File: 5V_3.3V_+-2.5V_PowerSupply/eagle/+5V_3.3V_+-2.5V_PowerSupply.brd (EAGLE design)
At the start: 100 x 80 mm, 55 parts, among them IC1 7805TV, IC2 LM4558N, IC3 TA48033S, SW1 PUSH_SW_ALT

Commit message: Update: 5V_3V3_2V5_PowerSupply Eagle Files
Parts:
- removed SL1: PWRIN+, con-amp-quick:02P
- removed SL2: PWRIN-, con-amp-quick:02P
- removed U$1, U$2: POLYSWITCH, mylib2:POLYSWITCH
- added JP21: TP_GND, pinhead:1X02
- added PS1, PS2: POLYSWITCH-5,0, mylib2:POLYSWITCH-5,0
- added X1: PWR-, con-wago-500:W237-102
- added X2: PWR+, con-wago-500:W237-102
- C1, C11, C2: device rcl:C050-025X075 -> rcl:C025-024X044
- C10, C9: device rcl:E2,5-6 -> rcl:E2,5-7
- C5: device rcl:C050-024X044 -> rcl:C025-024X044
- IC2: value LM4558N -> LM4556
- JP15, JP17, JP18, JP3, JP4: value +3.3V -> +2.5V
- LED1, LED4, LED5: value (none) -> GREEN
- LED2: value (none) -> RED
- LED3: value (none) -> BLUE
- moved JP20 310.4 mm to (86.4, 55.9), turned to 270 degrees
- moved JP19 302.5 mm to (83.8, 55.9), turned to 270 degrees
- moved LED5 243.2 mm to (50.8, 14.0), turned to 270 degrees
- moved R7 232.3 mm to (47.0, 10.2), turned to 180 degrees
- moved LED4 230.7 mm to (24.1, 30.5), turned to 180 degrees
- moved C6 224.6 mm to (47.0, 20.3), turned to 180 degrees
- moved JP18 222.0 mm to (86.4, 19.1), turned to 90 degrees
- moved R6 219.0 mm to (26.7, 10.2)
- moved JP15 213.0 mm to (81.3, 19.1), turned to 90 degrees
- moved JP17 209.6 mm to (83.8, 19.1), turned to 90 degrees
- moved C4 207.9 mm to (27.9, 19.1), turned to 270 degrees
- moved C2 205.4 mm to (45.7, 14.0), turned to 270 degrees
- moved JP3 203.9 mm to (76.2, 19.1), turned to 90 degrees
- moved JP4 200.5 mm to (78.7, 19.1), turned to 90 degrees
- moved C1 196.8 mm to (33.0, 19.1), turned to 270 degrees
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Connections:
- new net V+: C1.2, C2.1, C4.-, C6.+, IC2.1, IC2.2, JP15.1, JP17.1, JP18.1, JP3.1, JP4.1, LED5.A
- net +3V3: no longer C1.2, C2.1, C4.-, C6.+, IC2.1, IC2.2, JP15.1, JP17.1, JP18.1, JP3.1, JP4.1, LED5.A
- net +9V: now also JP19.1, JP20.1, R2.1; no longer LED2.A
- net -9V: now also JP19.3, JP20.3
- net GND: now also JP19.2, JP20.2, JP21.1, JP21.2, LED2.K, X1.1, X2.2; no longer R2.2, SL1.1, SL2.2
- net N$1: now also PS2.2, X2.1; no longer SL2.1, U$2.2
- net N$10: now also PS1.2, X1.2; no longer SL1.2, U$1.2
- net N$11: now also PS2.1, SW1.3; no longer SW1.4, U$2.1
- net N$2: now also PS1.1, SW1.6; no longer SW1.1, U$1.1
- net N$4: now also LED2.A, R2.2; no longer LED2.K, R2.1
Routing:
- net +9V: track 0.00 -> 5.08 mm
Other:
- board size 100 x 80 mm -> 93.7 x 71.1 mm

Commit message: Update: Eagle files
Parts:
- removed JP16, JP19, JP20: +-9V, pinhead:1X03
- removed JP17, JP18: +2.5V, pinhead:1X02
- JP10, JP9: value +3.3V -> +5V_2V5; device pinhead:1X02 -> pinhead:1X03
- JP13: value +5V -> +3.3V
- JP15: value +2.5V -> +3.3V
- JP3, JP4: value +2.5V -> +-9V; device pinhead:1X02 -> pinhead:1X03
- JP5: value +5V -> +-9V; device pinhead:1X02 -> pinhead:1X03
- JP6, JP7, JP8: value +5V -> +5V_2V5; device pinhead:1X02 -> pinhead:1X03
- moved JP3 30.2 mm to (68.6, 48.3), turned to 270 degrees
- moved JP4 30.2 mm to (71.1, 48.3), turned to 270 degrees
- moved JP13 23.4 mm to (68.6, 24.1), turned to 270 degrees
- moved R4 20.1 mm to (41.9, 10.2), turned to 180 degrees
- moved R6 19.1 mm to (25.4, 29.2), turned to 90 degrees
- moved JP11 18.5 mm to (63.5, 24.1), turned to 270 degrees
- moved JP12 18.5 mm to (66.0, 24.1), turned to 270 degrees
- moved JP10 16.5 mm to (63.5, 35.6), turned to 270 degrees
- moved JP14 16.1 mm to (71.1, 24.1), turned to 270 degrees
- moved JP8 15.7 mm to (68.6, 35.6), turned to 270 degrees
- moved JP1 14.8 mm to (63.5, 48.3)
- moved JP2 14.8 mm to (66.0, 48.3)
- moved C10 14.5 mm to (54.6, 53.3), turned to 0 degrees
- moved R7 13.7 mm to (59.7, 15.2)
- moved LED5 13.0 mm to (63.5, 11.4), turned to 90 degrees
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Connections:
- net +3V3: now also JP13.1, JP15.1; no longer JP10.1, JP9.1
- net +5V: now also JP10.1, JP9.1; no longer JP13.1, JP5.1
- net +9V: now also JP3.1, JP4.1, JP5.1; no longer JP16.1, JP19.1, JP20.1
- net -9V: now also JP3.3, JP4.3, JP5.3; no longer JP16.3, JP19.3, JP20.3
- net GND: now also JP10.3, JP6.3, JP7.3, JP8.3, JP9.3; no longer JP10.2, JP16.2, JP17.2, JP18.2, JP19.2, JP20.2, JP6.2, JP7.2, JP8.2, JP9.2
- net V+: now also JP10.2, JP6.2, JP7.2, JP8.2, JP9.2; no longer JP15.1, JP17.1, JP18.1, JP3.1, JP4.1
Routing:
- net GND: track 0.00 -> 374.2 mm
- net +5V: track 0.00 -> 159.8 mm, vias 0 -> 4
- net V+: track 0.00 -> 96.1 mm, vias 0 -> 2
- net -9V: track 0.00 -> 88.5 mm
- net +9V: track 5.08 -> 77.9 mm
- net +3V3: track 0.00 -> 63.1 mm, vias 0 -> 2
- net N$2: track 0.00 -> 20.3 mm
- net N$5: track 0.00 -> 17.3 mm
- net N$11: track 0.00 -> 12.2 mm
- net N$10: track 0.00 -> 5.25 mm
- net N$1: track 0.00 -> 5.25 mm
- net N$7: track 0.00 -> 5.08 mm
- net N$12: track 0.00 -> 2.54 mm
- net N$8: track 0.00 -> 2.54 mm
- net N$9: track 0.00 -> 2.54 mm
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
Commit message: Update: Board design
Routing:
- net +5V: track 159.8 -> 160.8 mm
- net V+: track 96.1 -> 97.1 mm
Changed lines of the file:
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@@
 <wire x1="35.56" y1="35.56" x2="40.64" y2="35.56" width="0.4064" layer="16"/>
 <wire x1="38.1" y1="20.32" x2="40.64" y2="20.32" width="0.4064" layer="16"/>
-<wire x1="33.02" y1="20.32" x2="30.48" y2="20.32" width="0.4064" layer="16"/>
-<wire x1="30.48" y1="20.32" x2="30.48" y2="15.24" width="0.4064" layer="16"/>
-<wire x1="30.48" y1="15.24" x2="35.56" y2="10.16" width="0.4064" layer="16"/>
-<wire x1="35.56" y1="10.16" x2="38.1" y2="10.16" width="0.4064" layer="16"/>
 <wire x1="33.02" y1="20.32" x2="38.1" y2="20.32" width="0.4064" layer="16"/>
-<wire x1="40.64" y1="20.32" x2="40.64" y2="22.86" width="0.4064" layer="16"/>
-<wire x1="40.64" y1="22.86" x2="22.86" y2="22.86" width="0.4064" layer="16"/>
 <wire x1="22.86" y1="22.86" x2="22.86" y2="35.56" width="0.4064" layer="1"/>
 <wire x1="22.86" y1="35.56" x2="35.56" y2="35.56" width="0.4064" layer="16"/>
@@
 <wire x1="48.26" y1="55.88" x2="50.8" y2="55.88" width="0.4064" layer="16"/>
 <wire x1="50.8" y1="55.88" x2="53.34" y2="53.34" width="0.4064" layer="16"/>
+<wire x1="38.1" y1="10.16" x2="30.48" y2="10.16" width="0.4064" layer="16"/>
+<wire x1="22.86" y1="22.86" x2="22.86" y2="20.32" width="0.4064" layer="16"/>
+<wire x1="22.86" y1="20.32" x2="22.86" y2="17.78" width="0.4064" layer="16"/>
+<wire x1="22.86" y1="17.78" x2="30.48" y2="10.16" width="0.4064" layer="16"/>
+<wire x1="38.1" y1="20.32" x2="22.86" y2="20.32" width="0.4064" layer="16"/>
 </signal>
 <signal name="+3V3">
@@
 <contactref element="C6" pad="+"/>
 <wire x1="43.18" y1="12.7" x2="40.64" y2="12.7" width="0.4064" layer="16"/>
-<wire x1="43.18" y1="12.7" x2="43.18" y2="5.08" width="0.4064" layer="16"/>
 <wire x1="43.18" y1="5.08" x2="48.26" y2="5.08" width="0.4064" layer="16"/>
 <wire x1="48.26" y1="5.08" x2="50.8" y2="7.62" width="0.4064" layer="16"/>
@@
 <wire x1="63.5" y1="35.56" x2="58.42" y2="35.56" width="0.4064" layer="16"/>
 <wire x1="58.42" y1="35.56" x2="58.42" y2="27.94" width="0.4064" layer="16"/>
+<wire x1="43.18" y1="5.08" x2="40.64" y2="7.62" width="0.4064" layer="16"/>
+<wire x1="40.64" y1="7.62" x2="40.64" y2="12.7" width="0.4064" layer="16"/>
 </signal>
 <signal name="N$2">

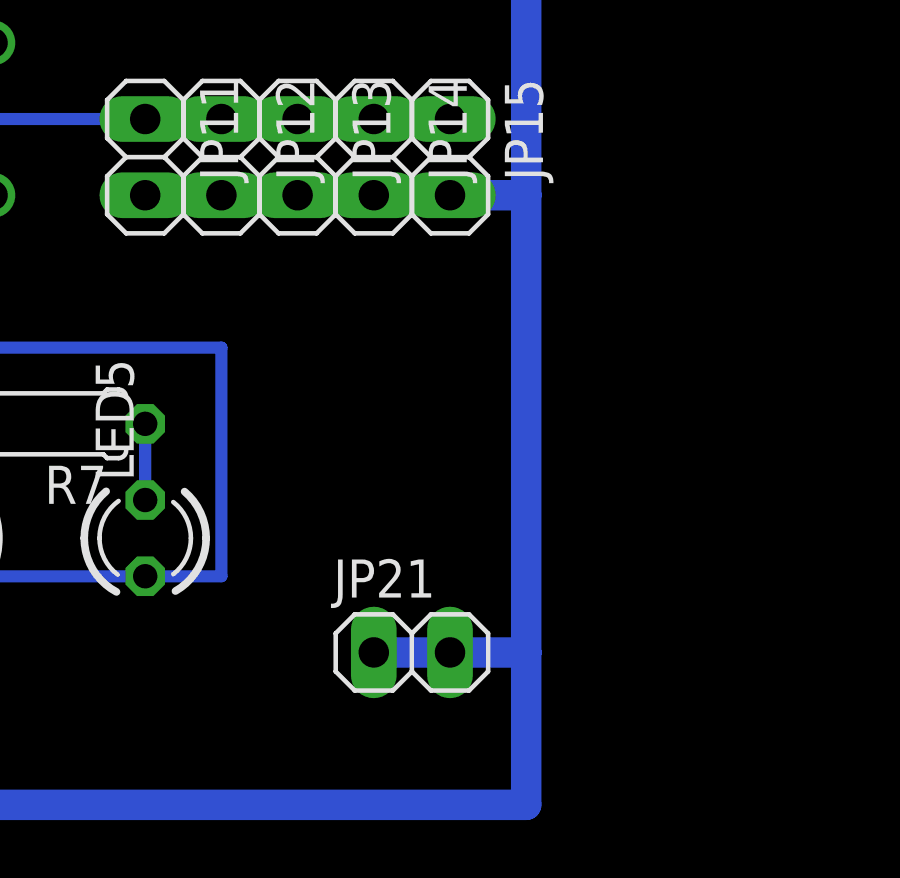
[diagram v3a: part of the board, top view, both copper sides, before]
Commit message: Add: 5V_3.3V_+-2.5V_PowerSupply Test Chart
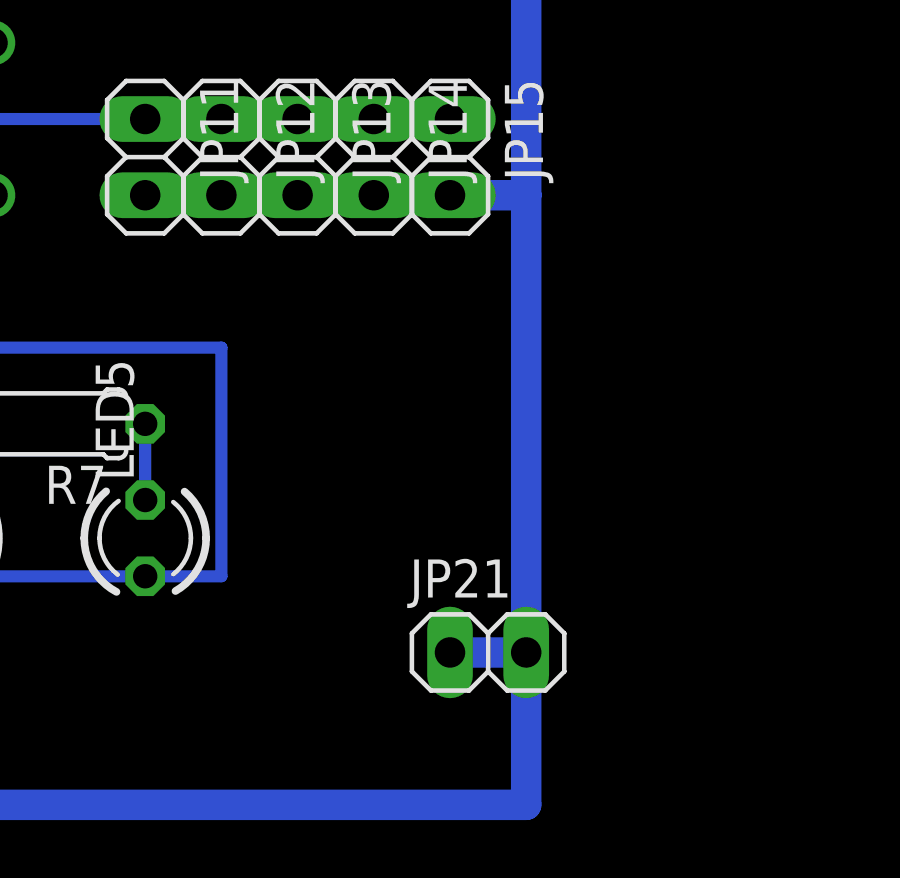
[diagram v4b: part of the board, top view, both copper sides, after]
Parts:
- moved JP21 2.54 mm to (74.9, 7.62)
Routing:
- net GND: track 374.2 -> 371.7 mm
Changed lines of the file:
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@@
 <attribute name="OC_FARNELL" value="unknown" x="8.89" y="53.34" size="1.778" layer="27" rot="R270" display="off"/>
 </element>
-<element name="JP21" library="pinhead" package="1X02" value="TP_GND" x="72.39" y="7.62"/>
+<element name="JP21" library="pinhead" package="1X02" value="TP_GND" x="74.93" y="7.62"/>
 <element name="SW1" library="mylib2" package="PUSH_SW_ALT" value="PUSH_SW_ALT" x="20.32" y="48.26"/>
 <element name="JP6" library="pinhead" package="1X03" value="+5V_2V5" x="73.66" y="35.56" rot="R270"/>
@@
 <wire x1="76.2" y1="40.64" x2="76.2" y2="33.02" width="1.016" layer="16"/>
 <wire x1="76.2" y1="33.02" x2="76.2" y2="22.86" width="1.016" layer="16"/>
-<wire x1="76.2" y1="22.86" x2="76.2" y2="7.62" width="1.016" layer="16"/>
-<wire x1="76.2" y1="7.62" x2="76.2" y2="2.54" width="1.016" layer="16"/>
 <wire x1="76.2" y1="2.54" x2="38.1" y2="2.54" width="1.016" layer="16"/>
 <wire x1="38.1" y1="2.54" x2="20.32" y2="2.54" width="1.016" layer="16"/>
-<wire x1="71.12" y1="7.62" x2="73.66" y2="7.62" width="1.016" layer="16"/>
+<wire x1="73.66" y1="7.62" x2="76.2" y2="7.62" width="1.016" layer="16"/>
 <wire x1="48.26" y1="25.4" x2="48.26" y2="20.32" width="1.016" layer="16"/>
 <wire x1="48.26" y1="20.32" x2="48.26" y2="12.7" width="1.016" layer="16"/>
-<wire x1="73.66" y1="7.62" x2="76.2" y2="7.62" width="1.016" layer="16"/>
 <wire x1="38.1" y1="7.62" x2="38.1" y2="2.54" width="1.016" layer="16"/>
 <wire x1="20.32" y1="2.54" x2="5.08" y2="17.78" width="1.016" layer="16"/>
@@
 <wire x1="71.12" y1="22.86" x2="68.58" y2="22.86" width="1.016" layer="16"/>
 <wire x1="73.66" y1="22.86" x2="71.12" y2="22.86" width="1.016" layer="16"/>
+<wire x1="76.2" y1="7.62" x2="76.2" y2="2.54" width="1.016" layer="16"/>
+<wire x1="76.2" y1="7.62" x2="76.2" y2="22.86" width="1.016" layer="16"/>
 </signal>
 <signal name="N$5">
